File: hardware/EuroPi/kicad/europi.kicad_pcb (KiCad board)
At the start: 2 copper layers, 85.7 x 110 mm, 92 parts, among them IC1 TL074, IC2 TL074, IC3 MCP6002, J1 Thonkiconn_Mono_Jack, J2 Thonkiconn_Mono_Jack, J3 Thonkiconn_Mono_Jack, J4 Thonkiconn_Mono_Jack, J5 Thonkiconn_Mono_Jack, J6 Thonkiconn_Mono_Jack, J7 Thonkiconn_Mono_Jack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

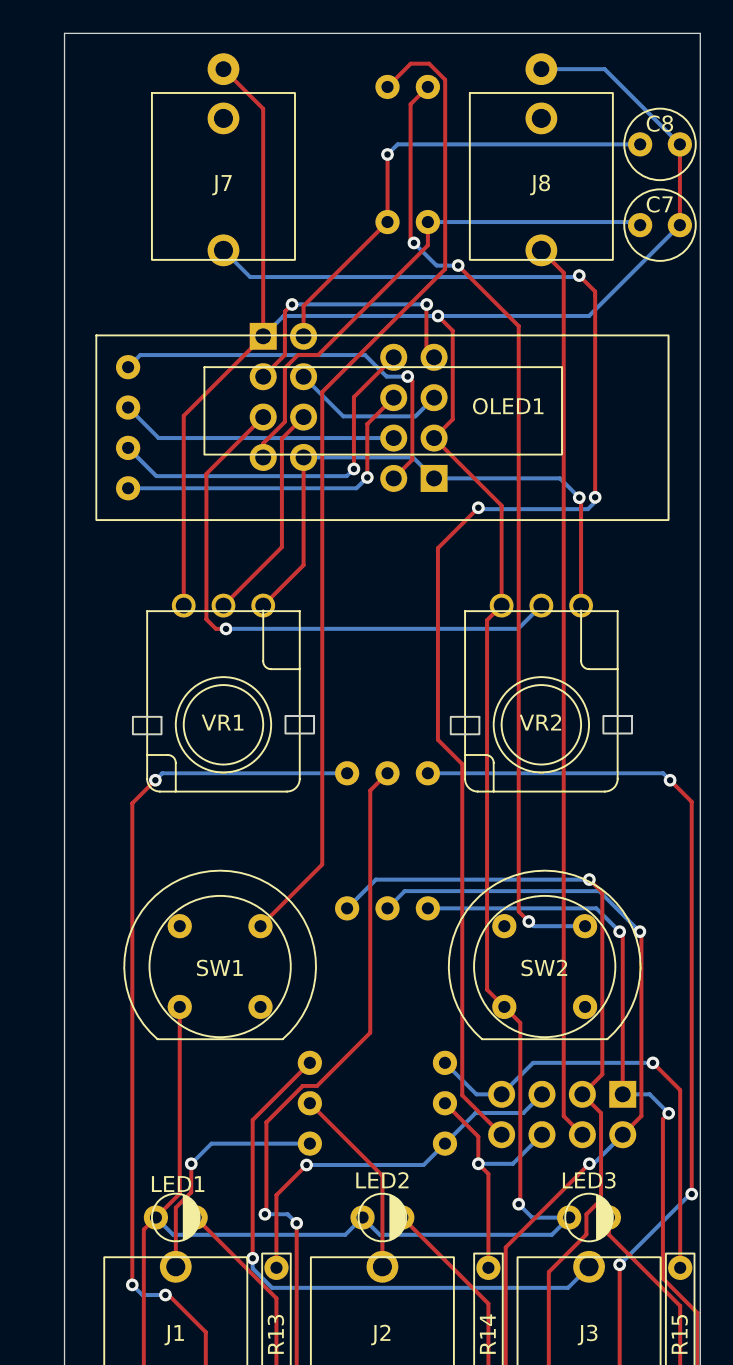
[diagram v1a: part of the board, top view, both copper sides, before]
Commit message: fix resistor sides, routing
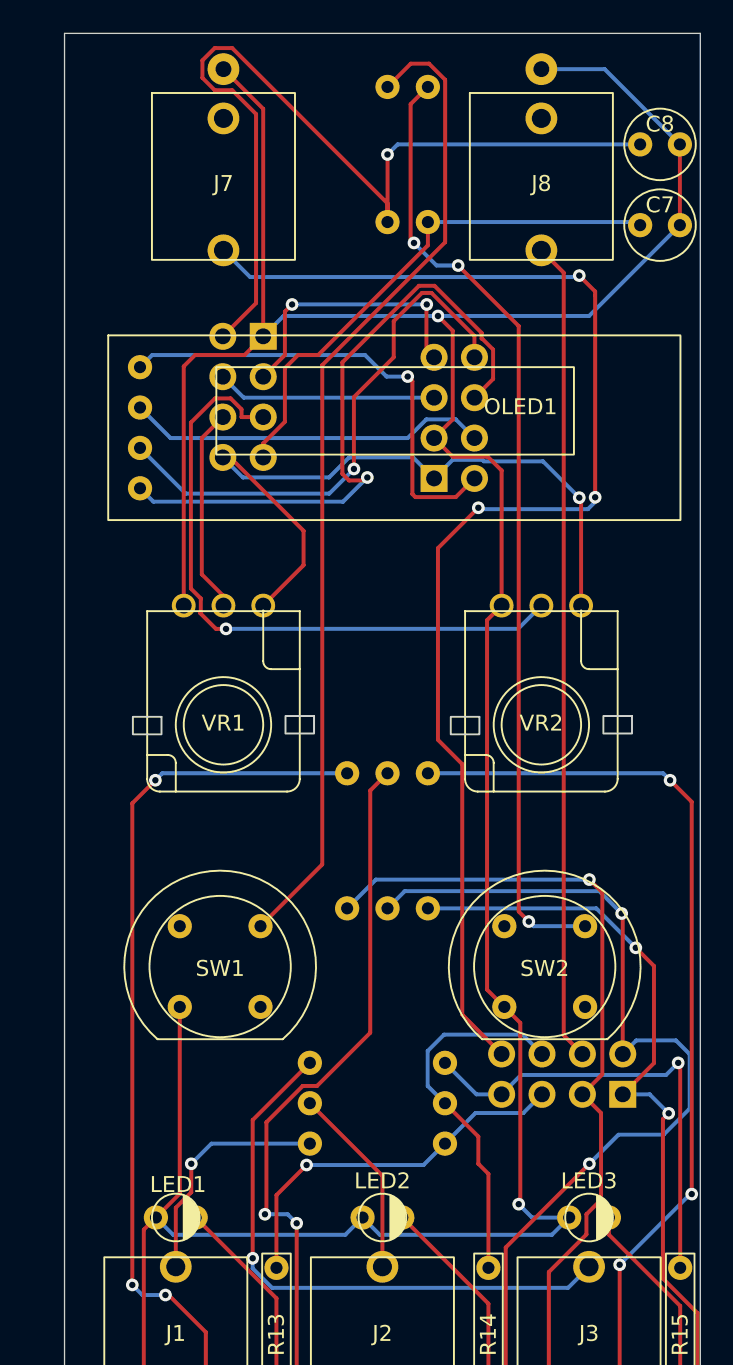
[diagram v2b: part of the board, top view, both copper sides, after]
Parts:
- CONN2, CONN4, CONN7: footprint Connector_PinSocket_2.54mm:PinSocket_2x04_P2.54mm_Vertical -> Connector_PinHeader_2.54mm:PinHeader_2x04_P2.54mm_Vertical
- D1, D2, D3, D4: value DIODE -> type="D" model="DIODE" lib=""
- R13, R14, R15, R16, R17, R18: value 1K -> 4K7
- moved OLED1 0.75 mm to (4.75, 21.0)
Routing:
- net /BUTTON 1 J: track 29.8 -> 57.9 mm
- net Net-(CONN7-Pin_6): track 21.0 -> 41.0 mm
- net Net-(CONN7-Pin_8): track 23.2 -> 33.9 mm
- net /+3.3V J: track 35.6 -> 45.1 mm
- net /OUTPUT 5 J: track 61.8 -> 69.0 mm
- net /OUTPUT 2 J: track 16.3 -> 23.4 mm, vias 1 -> 0
- net Net-(CONN7-Pin_4): track 17.5 -> 22.8 mm
- net /DIGITAL IN J: track 87.5 -> 82.4 mm
- net /ANALOGUE IN J: track 56.7 -> 51.6 mm
- net /KNOB 2 J: track 36.1 -> 40.7 mm
- net Net-(CONN7-Pin_2): track 25.5 -> 29.7 mm
- net /OLED SCL J: track 9.73 -> 13.8 mm
- net /EARTH J: track 286.5 -> 289.7 mm
- net /OUTPUT 6 J: track 56.6 -> 58.3 mm
- net /OUTPUT 3 J: track 28.3 -> 29.3 mm
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
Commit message: kicad save
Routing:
- added copper zone on B.Cu, net /EARTH J
- added copper zone on B.Cu, net Earth
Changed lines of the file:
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@@
   (segment (start 10 36) (end 10.3 35.7) (width 0.25) (layer "F.Cu") (net 107))
   (segment (start 8.636 34.036) (end 8.636 25.464) (width 0.25) (layer "F.Cu") (net 107))
+  (zone (net 1) (net_name "Earth") (layer "B.Cu") (hatch edge 0.5)
+    (priority 1)
+    (connect_pads (clearance 0.508))
+    (min_thickness 0.25) (filled_areas_thickness no)
+    (fill yes (thermal_gap 0.5) (thermal_bridge_width 0.5))
+    (polygon
+      (pts
+        (xy -45.72 0)
+        (xy -5.08 0)
+        (xy -5.08 110.236)
+        (xy -45.72 110.236)
+      )
+    )
+  )
+  (zone (net 105) (net_name "/EARTH J") (layer "B.Cu") (hatch edge 0.5)
+    (connect_pads (clearance 0.508))
+    (min_thickness 0.25) (filled_areas_thickness no)
+    (fill yes (thermal_gap 0.5) (thermal_bridge_width 0.5))
+    (polygon
+      (pts
+        (xy 0 0)
+        (xy 40.132 0)
+        (xy 40.132 110.236)
+        (xy 0 110.236)
+      )
+    )
+  )
 )
